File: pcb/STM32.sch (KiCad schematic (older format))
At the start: 10 parts, among them U5 STM32F103ZE

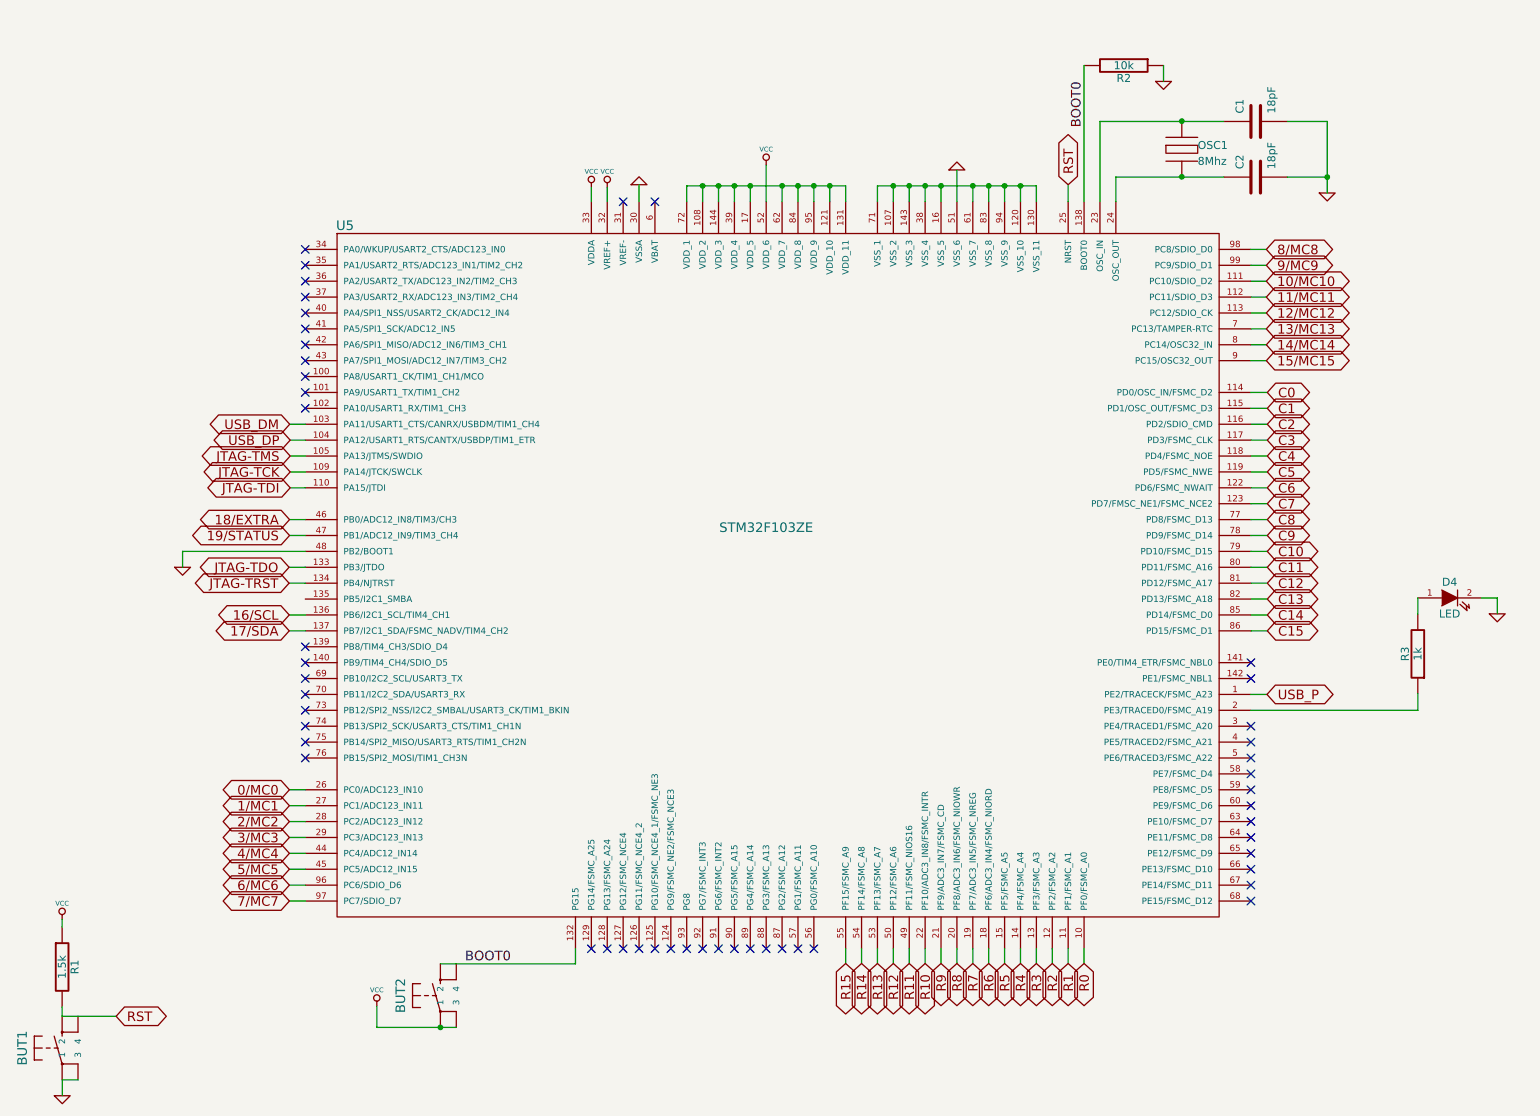
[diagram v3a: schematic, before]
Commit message: Re-routing new, single-board PCB
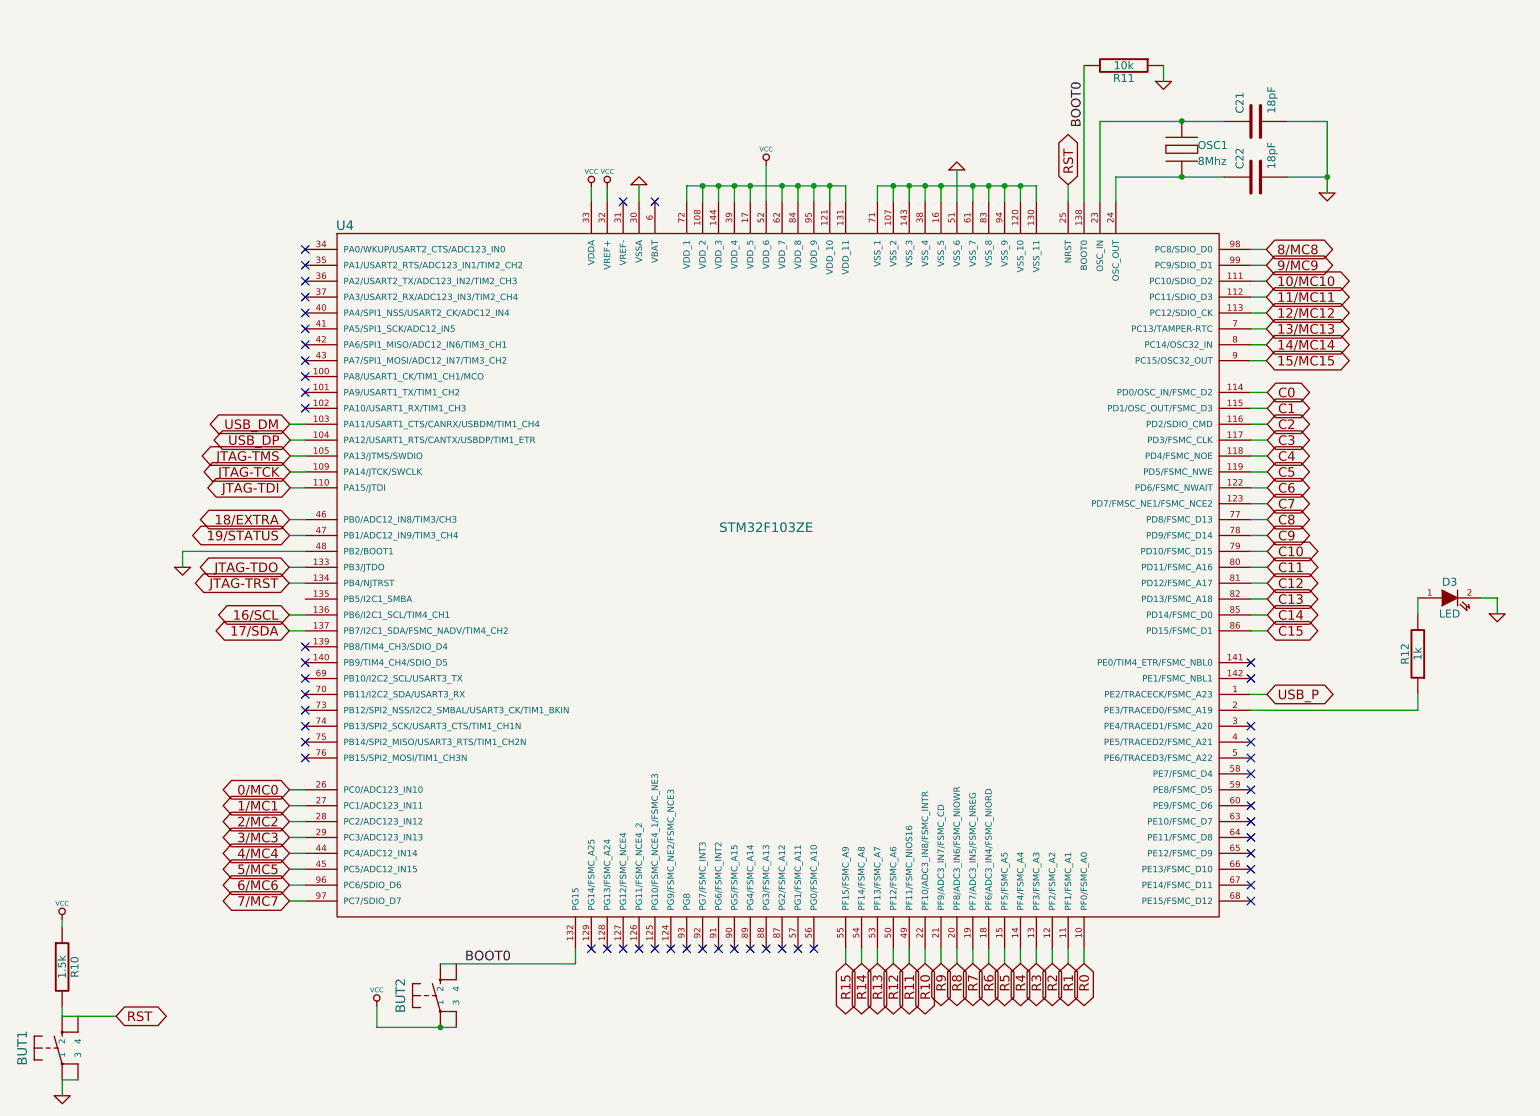
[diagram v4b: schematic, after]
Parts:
- renumbered C1 to C21, C2 to C22, D4 to D3, R1 to R10, R2 to R11, R3 to R12, U5 to U4
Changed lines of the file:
@@
-EESchema Schematic File Version 2  date Tue 12 Mar 2013 12:36:21 PM PDT
+EESchema Schematic File Version 2  date Wed 20 Mar 2013 06:41:12 PM PDT
 LIBS:power
 LIBS:device
@@
 Sheet 5 5
 Title ""
-Date "12 mar 2013"
+Date "21 mar 2013"
 Rev ""
 Comp ""
@@
 	5030 1700 5030 1610
 $Comp
-L VCC #PWR?
+L VCC #PWR027
 U 1 1 513F826F
 P 5030 1610
-F 0 "#PWR?" H 5030 1710 30  0001 C CNN
+F 0 "#PWR027" H 5030 1710 30  0001 C CNN
 F 1 "VCC" H 5030 1710 30  0000 C CNN
 	1    5030 1610
@@
 $EndComp
 $Comp
-L VCC #PWR?
+L VCC #PWR028
 U 1 1 513F825E
 P 4930 1610
-F 0 "#PWR?" H 4930 1710 30  0001 C CNN
+F 0 "#PWR028" H 4930 1710 30  0001 C CNN
 F 1 "VCC" H 4930 1710 30  0000 C CNN
 	1    4930 1610
@@
 Connection ~ 9560 1545
 Wire Wire Line
-	9560 1645 9560 1545
-Wire Wire Line
-	9560 1545 9560 1195
+	9560 1645 9560 1195
 Wire Wire Line
 	8230 1700 8230 1545
@@
 	4830 6495 4830 6400
 Wire Wire Line
-	5530 1600 5630 1600
-Wire Wire Line
-	5630 1600 5730 1600
-Wire Wire Line
-	5730 1600 5830 1600
-Wire Wire Line
-	5830 1600 5930 1600
-Wire Wire Line
-	5930 1600 6130 1600
-Wire Wire Line
-	6130 1600 6230 1600
-Wire Wire Line
-	6230 1600 6330 1600
-Wire Wire Line
-	6330 1600 6430 1600
-Wire Wire Line
-	6430 1600 6530 1600
+	5530 1600 6530 1600
 Wire Wire Line
 	5530 1600 5530 1700
@@
 	6330 1600 6330 1700
 Wire Wire Line
-	6730 1600 6830 1600
-Wire Wire Line
-	6830 1600 6930 1600
-Wire Wire Line
-	6930 1600 7030 1600
-Wire Wire Line
-	7030 1600 7130 1600
-Wire Wire Line
-	7130 1600 7330 1600
-Wire Wire Line
-	7330 1600 7430 1600
-Wire Wire Line
-	7430 1600 7530 1600
-Wire Wire Line
-	7530 1600 7630 1600
-Wire Wire Line
-	7630 1600 7730 1600
+	6730 1600 7730 1600
 Connection ~ 7630 1600
 Wire Wire Line
@@
 	6030 1700 6030 1470
 Wire Wire Line
-	3580 6895 3980 6895
-Wire Wire Line
-	3980 6895 4080 6895
+	3580 6895 4080 6895
 Connection ~ 3980 6895
 Wire Wire Line
@@
 U 1 1 4BB523CB
 P 1600 7025
-AR Path="/51099A3F/4BB523CB" Ref="BUT1"  Part="1"
-AR Path="/510998BD/4BB523CB" Ref="BUT1"  Part="1"
 F 0 "BUT1" H 1600 7275 60  0000 C CNN
 F 1 "BUT" H 1600 7275 60  0001 C CNN
@@
 U 1 1 4BB523D5
 P 3980 6695
-AR Path="/51099A3F/4BB523D5" Ref="BUT2"  Part="1"
-AR Path="/510998BD/4BB523D5" Ref="BUT2"  Part="1"
 F 0 "BUT2" H 3980 6945 60  0000 C CNN
 F 1 "BUT" H 3980 6945 60  0001 C CNN
@@
 $EndComp
 $Comp
-L R R3
+L R R12
 U 1 1 510B216F
 P 10130 4545
-F 0 "R3" V 10210 4545 50  0000 C CNN
+F 0 "R12" V 10210 4545 50  0000 C CNN
 F 1 "1k" V 10130 4545 50  0000 C CNN
 F 4 "P1.0KJCT-ND" V 10130 4545 60  0001 C CNN "Digikey P/N"
@@
 $EndComp
 $Comp
-L LED D4
+L LED D3
 U 1 1 510B216E
 P 10330 4193
-F 0 "D4" H 10330 4293 50  0000 C CNN
+F 0 "D3" H 10330 4293 50  0000 C CNN
 F 1 "LED" H 10330 4093 50  0000 C CNN
 F 4 "P13484CT-ND" H 10330 4193 60  0001 C CNN "Digikey P/N"
@@
 $EndComp
 $Comp
-L GND #PWR028
+L GND #PWR029
 U 1 1 510B216D
 P 10630 4293
-F 0 "#PWR028" H 10630 4293 30  0001 C CNN
+F 0 "#PWR029" H 10630 4293 30  0001 C CNN
 F 1 "GND" H 10630 4223 30  0001 C CNN
 	1    10630 4293
@@
 $EndComp
 $Comp
-L STM32F103ZE U5
+L STM32F103ZE U4
 U 1 1 5109CC02
 P 6030 3750
-F 0 "U5" H 3380 5650 60  0000 C CNN
+F 0 "U4" H 3380 5650 60  0000 C CNN
 F 1 "STM32F103ZE" H 6030 3750 60  0000 C CNN
 	1    6030 3750
@@
 $EndComp
 $Comp
-L GND #PWR029
+L GND #PWR030
 U 1 1 510B1EA9
 P 7230 1500
-F 0 "#PWR029" H 7230 1500 30  0001 C CNN
+F 0 "#PWR030" H 7230 1500 30  0001 C CNN
 F 1 "GND" H 7230 1430 30  0001 C CNN
 	1    7230 1500
@@
 $EndComp
 $Comp
-L VCC #PWR030
+L VCC #PWR031
 U 1 1 510B1E7E
 P 6030 1470
-F 0 "#PWR030" H 6030 1570 30  0001 C CNN
+F 0 "#PWR031" H 6030 1570 30  0001 C CNN
 F 1 "VCC" H 6030 1570 30  0000 C CNN
 	1    6030 1470
@@
 $EndComp
 $Comp
-L GND #PWR031
+L GND #PWR032
 U 1 1 510B1E3A
 P 5230 1593
-F 0 "#PWR031" H 5230 1593 30  0001 C CNN
+F 0 "#PWR032" H 5230 1593 30  0001 C CNN
 F 1 "GND" H 5230 1523 30  0001 C CNN
 	1    5230 1593
@@
 JTAG-TRST
 $Comp
-L GND #PWR032
+L GND #PWR033
 U 1 1 510B1B6F
 P 2358 4000
-F 0 "#PWR032" H 2358 4000 30  0001 C CNN
+F 0 "#PWR033" H 2358 4000 30  0001 C CNN
 F 1 "GND" H 2358 3930 30  0001 C CNN
 	1    2358 4000
@@
 BOOT0
 $Comp
-L VCC #PWR061
+L VCC #PWR034
 U 1 1 4B8ADEC7
 P 3580 6760
-AR Path="/51099A3F/4B8ADEC7" Ref="#PWR061"  Part="1"
-AR Path="/510998BD/4B8ADEC7" Ref="#PWR033"  Part="1"
-F 0 "#PWR033" H 3580 6860 30  0001 C CNN
+F 0 "#PWR034" H 3580 6860 30  0001 C CNN
 F 1 "VCC" H 3580 6860 30  0000 C CNN
 	1    3580 6760
@@
 U 1 1 4B8383C6
 P 8645 1395
-AR Path="/51099A3F/4B8383C6" Ref="OSC1"  Part="1"
-AR Path="/510998BD/4B8383C6" Ref="OSC1"  Part="1"
 F 0 "OSC1" H 8745 1445 50  0000 L CNN
 F 1 "8Mhz" H 8745 1345 50  0000 L CNN
@@
 $EndComp
 $Comp
-L GND #PWR062
+L GND #PWR035
 U 1 1 4B8383A4
 P 9560 1645
-AR Path="/51099A3F/4B8383A4" Ref="#PWR062"  Part="1"
-AR Path="/510998BD/4B8383A4" Ref="#PWR034"  Part="1"
-F 0 "#PWR034" H 9560 1645 30  0001 C CNN
+F 0 "#PWR035" H 9560 1645 30  0001 C CNN
 F 1 "GND" H 9560 1575 30  0001 C CNN
 	1    9560 1645
@@
 $EndComp
 $Comp
-L C C2
+L C C22
 U 1 1 4B837588
 P 9110 1545
-AR Path="/51099A3F/4B837588" Ref="C2"  Part="1"
-AR Path="/510998BD/4B837588" Ref="C2"  Part="1"
-F 0 "C2" H 9160 1645 50  0000 L CNN
+F 0 "C22" H 9160 1645 50  0000 L CNN
 F 1 "18pF" H 9160 1445 50  0000 L CNN
 F 4 "587-1950-1-ND" H 9110 1545 60  0001 C CNN "Digikey P/N"
@@
 $EndComp
 $Comp
-L C C1
+L C C21
 U 1 1 4B837587
 P 9110 1195
-AR Path="/51099A3F/4B837587" Ref="C1"  Part="1"
-AR Path="/510998BD/4B837587" Ref="C1"  Part="1"
-F 0 "C1" H 9160 1295 50  0000 L CNN
+F 0 "C21" H 9160 1295 50  0000 L CNN
 F 1 "18pF" H 9160 1095 50  0000 L CNN
 F 4 "587-1950-1-ND" H 9110 1195 60  0001 C CNN "Digikey P/N"
@@
 $EndComp
 $Comp
-L GND #PWR063
+L GND #PWR036
 U 1 1 4B83757E
 P 8530 943
-AR Path="/51099A3F/4B83757E" Ref="#PWR063"  Part="1"
-AR Path="/510998BD/4B83757E" Ref="#PWR035"  Part="1"
-F 0 "#PWR035" H 8530 943 30  0001 C CNN
+F 0 "#PWR036" H 8530 943 30  0001 C CNN
 F 1 "GND" H 8530 873 30  0001 C CNN
 	1    8530 943
@@
 $EndComp
 $Comp
-L R R2
+L R R11
 U 1 1 4B83757D
 P 8280 843
-AR Path="/51099A3F/4B83757D" Ref="R2"  Part="1"
-AR Path="/510998BD/4B83757D" Ref="R2"  Part="1"
-F 0 "R2" V 8360 843 50  0000 C CNN
+F 0 "R11" V 8360 843 50  0000 C CNN
 F 1 "10k" V 8280 843 50  0000 C CNN
 F 4 "311-10KJRCT-ND" V 8280 843 60  0001 C CNN "Digikey P/N"
@@
 $EndComp
 $Comp
-L GND #PWR064
+L GND #PWR037
 U 1 1 4B83757C
 P 1601 7325
-AR Path="/51099A3F/4B83757C" Ref="#PWR064"  Part="1"
-AR Path="/510998BD/4B83757C" Ref="#PWR036"  Part="1"
-F 0 "#PWR036" H 1601 7325 30  0001 C CNN
+F 0 "#PWR037" H 1601 7325 30  0001 C CNN
 F 1 "GND" H 1601 7255 30  0001 C CNN
 	1    1601 7325
@@
 $EndComp
 $Comp
-L VCC #PWR065
+L VCC #PWR038
 U 1 1 4B83757A
 P 1600 6215
-AR Path="/51099A3F/4B83757A" Ref="#PWR065"  Part="1"
-AR Path="/510998BD/4B83757A" Ref="#PWR037"  Part="1"
-F 0 "#PWR037" H 1600 6315 30  0001 C CNN
+F 0 "#PWR038" H 1600 6315 30  0001 C CNN
 F 1 "VCC" H 1600 6315 30  0000 C CNN
 	1    1600 6215
@@
 $EndComp
 $Comp
-L R R1
+L R R10
 U 1 1 4B837579
 P 1600 6515
-AR Path="/51099A3F/4B837579" Ref="R1"  Part="1"
-AR Path="/510998BD/4B837579" Ref="R1"  Part="1"
-F 0 "R1" V 1680 6515 50  0000 C CNN
+F 0 "R10" V 1680 6515 50  0000 C CNN
 F 1 "1.5k" V 1600 6515 50  0000 C CNN
 F 4 "445-4952-1-ND" V 1600 6515 60  0001 C CNN "Digikey P/N"

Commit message: Board is routed!
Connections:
- net at C21.1, U4.23 (OSC_IN): now also OSC1.1
- net at C22.1, U4.24 (OSC_OUT): now also OSC1.3
- net DISC: now reaches U4.139 (PB8/TIM4_CH3/SDIO_D4)
- no-connect marks 50 -> 49
